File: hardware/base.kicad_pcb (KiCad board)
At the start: 4 copper layers, 100 x 85 mm, 316 parts, among them J101 USB-A, J102 TNG-Data-TOP, J103 TNG-Power-TOP, J301 MICROSDCARD, J302 Raspberry-Pi-Compute-Socket, J303 MICRO_HDMI, J304 USB Micro, J401 RJSLG-001TA1, P101 Debug, P102 Boot, P103 PE, P104 TST_GND, P105 TST_3V3P, P201 DI IN, P202 PWR IN, P203 TST_5V, P204 TST_GND, P301 TST_XMC_10, P302 TST_SCL, P303 TST_SDA, P304 TST_WP, P305 TST_3V3, P306 TST_1V8, P307 TST_XMC_11, P401 TST_1V2, Q301 2N7002P, Q302 2N7002P, Q303 2N7002P, Q304 2N7002P, Q305 2N7002P, T201 744272251, U101 USB2517, U102 MIC2026-1YM, U103 82400152, U104 XMC1XXX24, U105 TPD4S010DQA, U106 TPD4S010DQA, U107 TPD4S010DQA, U108 AP7333-33SAG-7, U109 TPS22975, U110 TPS22975, U111 PCT2075DP, U112 VN7140AS, U201 ISO1211, U202 FPF2700MX, U203 BD90640HFP, U204 PAC1933, U301 PAM2306AYPAA, U302 PCF8523T, U303 FSUSB42MUX, U304 TPD4S010DQA, U305 TPD4S010DQA, U306 TPD4S010DQA, U307 82400152, U308 M24256-DFMN6TP, U309 AP2331, U310 SLB9670, U401 LAN7500, U402 93AA66, U403 TPD4S010DQA, U404 TPD4S010DQA, U405 PAM2306AYPAA, X101 24MHz, X301 32.768kHz, X401 25MHz_18pF

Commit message: fix text
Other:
- board text added: "BASE RPI CMX REV 1.2"
- board text removed: "Base RPI CMX REV 1.2"

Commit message: specify capacitor voltages
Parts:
- C201, C202: value 10uF -> 10uF/35V
- C205: value 100nF -> 100nF/35V

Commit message: fix capacitor footprints
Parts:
- C135, C136: footprint C1206 -> kicad-libraries:C0805E
- C203: value 10uF -> 10uF/35V
- C219: value >100µF -> 100µF
- moved C135 0.40 mm to (153.7, 78.4)
- moved C136 0.40 mm to (153.7, 80.6)

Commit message: fix capacitor values
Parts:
- C108, C109, C117: value >100uF -> 100uF
- C216, C220: value >100µF -> 100µF

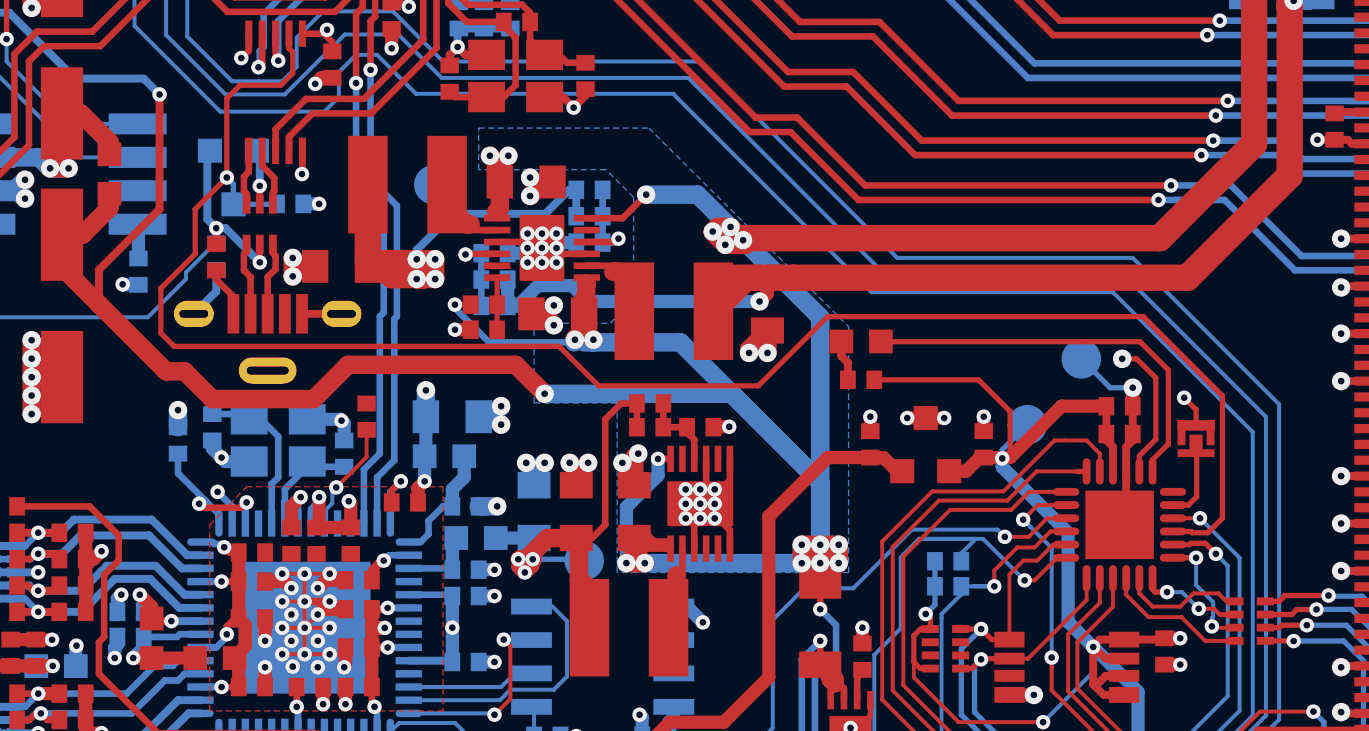
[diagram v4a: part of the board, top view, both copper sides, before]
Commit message: fix footprints
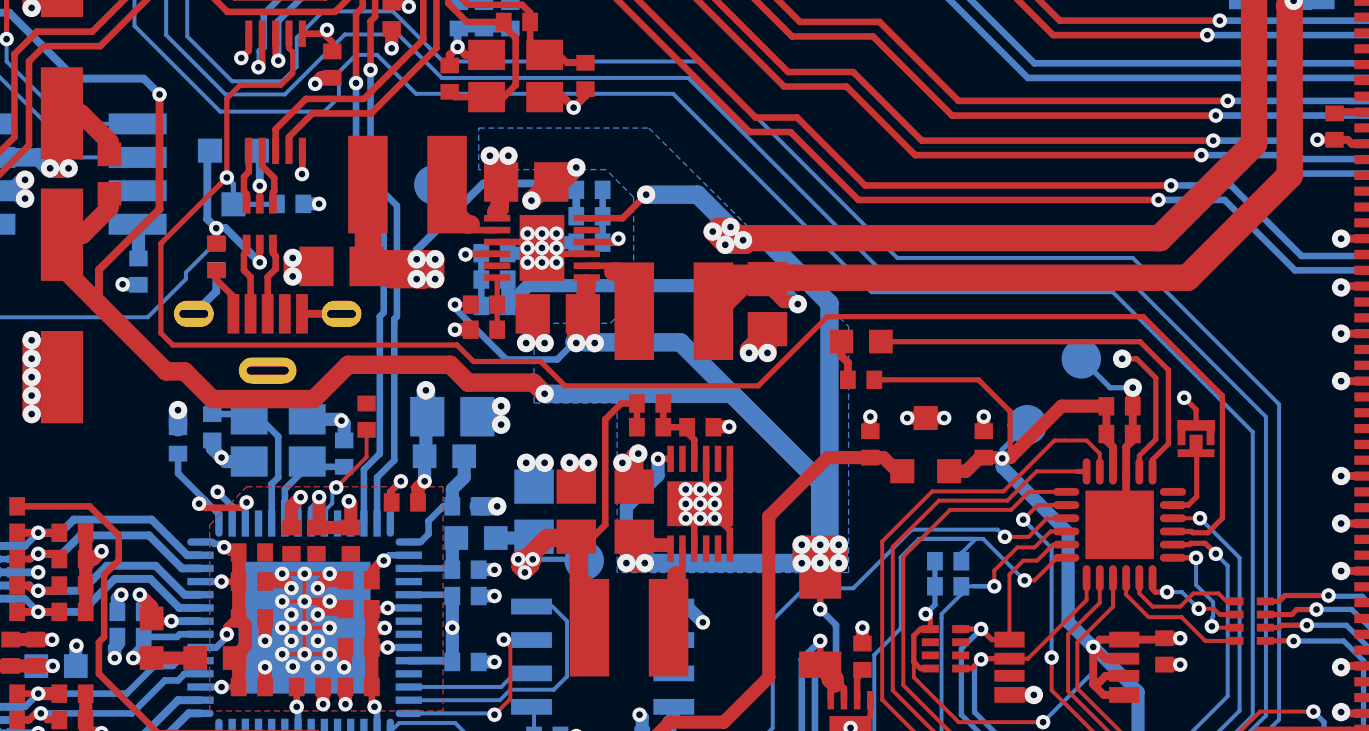
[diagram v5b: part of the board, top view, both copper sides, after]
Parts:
- C301, C303, C309, C311, C401, C410, C435, C437: footprint C0805 -> kicad-libraries:C0805E
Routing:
- net +1.8V: track 124.2 -> 126.4 mm
- net 5VSW: track 251.9 -> 253.4 mm
- net AGND: track 1114.5 -> 1115.5 mm

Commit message: fix footprint
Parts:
- R118: footprint kicad-libraries:1206 -> kicad-libraries:R1206

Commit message: fix values
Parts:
- C127, C128, C307, C308, C310, C320: value 1µF -> 1uF
- C216, C219, C220: value 100µF -> 100uF
- C301, C303, C309, C311, C435, C437: value 10µF -> 10uF
- C304, C312, C313, C314: value 47µF -> 47uF
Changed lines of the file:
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@@
       (effects (font (size 0.3 0.3) (thickness 0.075)) (justify mirror))
     )
-    (fp_text value 47µF (at 0 0.65 180) (layer B.Fab)
+    (fp_text value 47uF (at 0 0.65 180) (layer B.Fab)
       (effects (font (size 0.3 0.3) (thickness 0.075)) (justify mirror))
     )
@@
       (effects (font (size 0.3 0.3) (thickness 0.075)) (justify mirror))
     )
-    (fp_text value 47µF (at 0 0.65 180) (layer B.Fab)
+    (fp_text value 47uF (at 0 0.65 180) (layer B.Fab)
       (effects (font (size 0.3 0.3) (thickness 0.075)) (justify mirror))
     )
@@
       (effects (font (size 0.3 0.3) (thickness 0.075)) (justify mirror))
     )
-    (fp_text value 47µF (at 0 0.65 180) (layer B.Fab)
+    (fp_text value 47uF (at 0 0.65 180) (layer B.Fab)
       (effects (font (size 0.3 0.3) (thickness 0.075)) (justify mirror))
     )
@@
       (effects (font (size 0.2 0.2) (thickness 0.05)))
     )
-    (fp_text value 1µF (at 0 -0.15 270) (layer F.Fab)
+    (fp_text value 1uF (at 0 -0.15 270) (layer F.Fab)
       (effects (font (size 0.2 0.2) (thickness 0.05)))
     )
@@
       (effects (font (size 0.2 0.2) (thickness 0.05)))
     )
-    (fp_text value 1µF (at 0 -0.15) (layer F.Fab)
+    (fp_text value 1uF (at 0 -0.15) (layer F.Fab)
       (effects (font (size 0.2 0.2) (thickness 0.05)))
     )
@@
       (effects (font (size 0.59944 0.59944) (thickness 0.12446)))
     )
-    (fp_text value 100µF (at 0.95 -0.375 90) (layer F.Fab)
+    (fp_text value 100uF (at 0.95 -0.375 90) (layer F.Fab)
       (effects (font (size 0.59944 0.59944) (thickness 0.12446)))
     )
@@
       (effects (font (size 0.59944 0.59944) (thickness 0.12446)))
     )
-    (fp_text value 100µF (at 0.95 -0.375 90) (layer F.Fab)
+    (fp_text value 100uF (at 0.95 -0.375 90) (layer F.Fab)
       (effects (font (size 0.59944 0.59944) (thickness 0.12446)))
     )
@@
       (effects (font (size 0.59944 0.59944) (thickness 0.12446)))
     )
-    (fp_text value 100µF (at 0.95 -0.375 90) (layer F.Fab)
+    (fp_text value 100uF (at 0.95 -0.375 90) (layer F.Fab)
       (effects (font (size 0.59944 0.59944) (thickness 0.12446)))
     )
@@
       (effects (font (size 0.2 0.2) (thickness 0.05)))
     )
-    (fp_text value 1µF (at 0.05 -0.375 90) (layer F.Fab)
+    (fp_text value 1uF (at 0.05 -0.375 90) (layer F.Fab)
       (effects (font (size 0.2 0.2) (thickness 0.05)))
     )
@@
       (effects (font (size 0.2 0.2) (thickness 0.05)))
     )
-    (fp_text value 1µF (at 0 -0.15 90) (layer F.Fab)
+    (fp_text value 1uF (at 0 -0.15 90) (layer F.Fab)
       (effects (font (size 0.2 0.2) (thickness 0.05)))
     )
@@
       (effects (font (size 0.2 0.2) (thickness 0.05)))
     )
-    (fp_text value 1µF (at 0 -0.15 90) (layer F.Fab)
+    (fp_text value 1uF (at 0 -0.15 90) (layer F.Fab)
       (effects (font (size 0.2 0.2) (thickness 0.05)))
     )
@@
       (effects (font (size 0.2 0.2) (thickness 0.05)))
     )
-    (fp_text value 1µF (at 0 -0.15 90) (layer F.Fab)
+    (fp_text value 1uF (at 0 -0.15 90) (layer F.Fab)
       (effects (font (size 0.2 0.2) (thickness 0.05)))
     )
@@
       (effects (font (size 0.2 0.2) (thickness 0.05)))
     )
-    (fp_text value 47µF (at 0 -0.4 90) (layer F.Fab)
+    (fp_text value 47uF (at 0 -0.4 90) (layer F.Fab)
       (effects (font (size 0.2 0.2) (thickness 0.05)))
     )
@@
       (effects (font (size 0.2 0.2) (thickness 0.05)))
     )
-    (fp_text value 10µF (at 0 -0.4) (layer F.Fab)
+    (fp_text value 10uF (at 0 -0.4) (layer F.Fab)
       (effects (font (size 0.2 0.2) (thickness 0.05)))
     )
@@
       (effects (font (size 0.2 0.2) (thickness 0.05)))
     )
-    (fp_text value 10µF (at 0 -0.4 90) (layer F.Fab)
+    (fp_text value 10uF (at 0 -0.4 90) (layer F.Fab)
       (effects (font (size 0.2 0.2) (thickness 0.05)))
     )
@@
       (effects (font (size 0.2 0.2) (thickness 0.05)))
     )
-    (fp_text value 10µF (at 0 -0.4 90) (layer F.Fab)
+    (fp_text value 10uF (at 0 -0.4 90) (layer F.Fab)
       (effects (font (size 0.2 0.2) (thickness 0.05)))
     )
@@
       (effects (font (size 0.2 0.2) (thickness 0.05)))
     )
-    (fp_text value 10µF (at 0 -0.4) (layer F.Fab)
+    (fp_text value 10uF (at 0 -0.4) (layer F.Fab)
       (effects (font (size 0.2 0.2) (thickness 0.05)))
     )
@@
       (effects (font (size 0.2 0.2) (thickness 0.05)))
     )
-    (fp_text value 10µF (at 0 -0.4) (layer F.Fab)
+    (fp_text value 10uF (at 0 -0.4) (layer F.Fab)
       (effects (font (size 0.2 0.2) (thickness 0.05)))
     )
@@
       (effects (font (size 0.2 0.2) (thickness 0.05)))
     )
-    (fp_text value 10µF (at 0 -0.4 90) (layer F.Fab)
+    (fp_text value 10uF (at 0 -0.4 90) (layer F.Fab)
       (effects (font (size 0.2 0.2) (thickness 0.05)))
     )

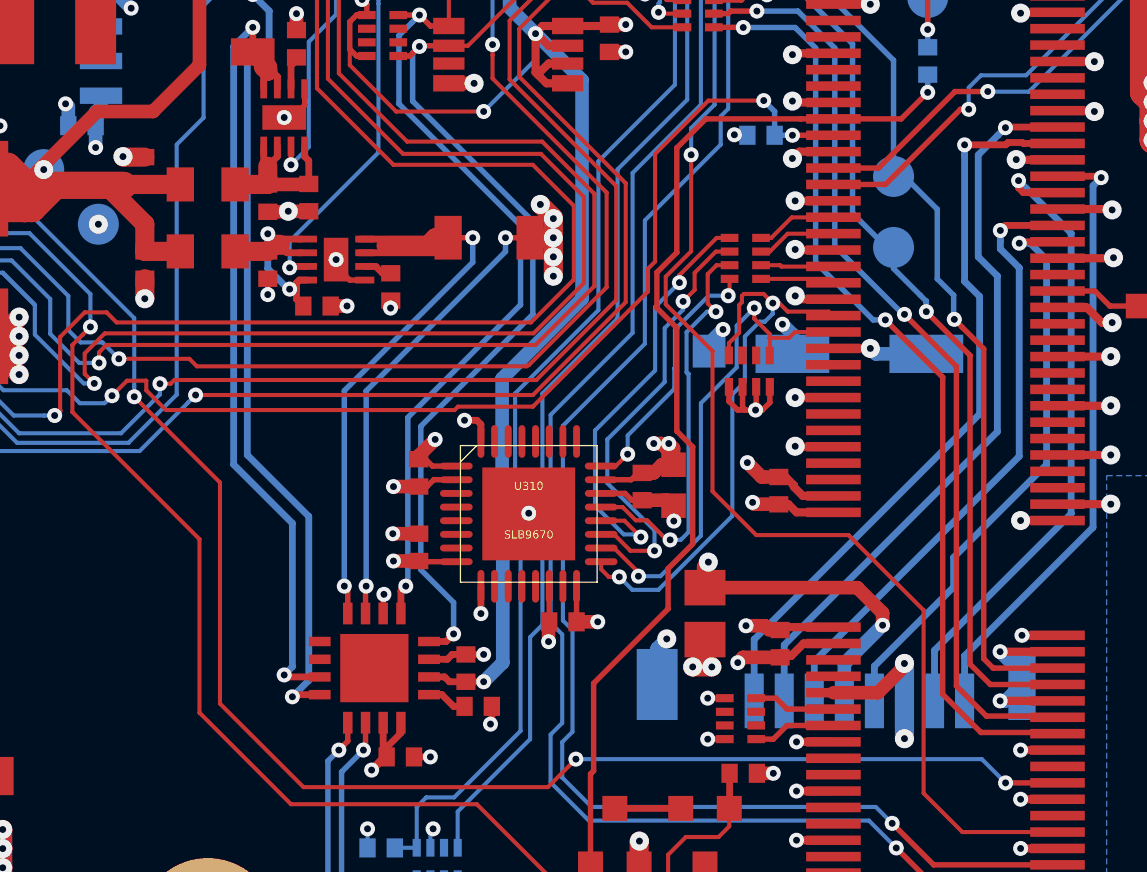
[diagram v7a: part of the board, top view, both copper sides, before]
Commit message: fix footprints
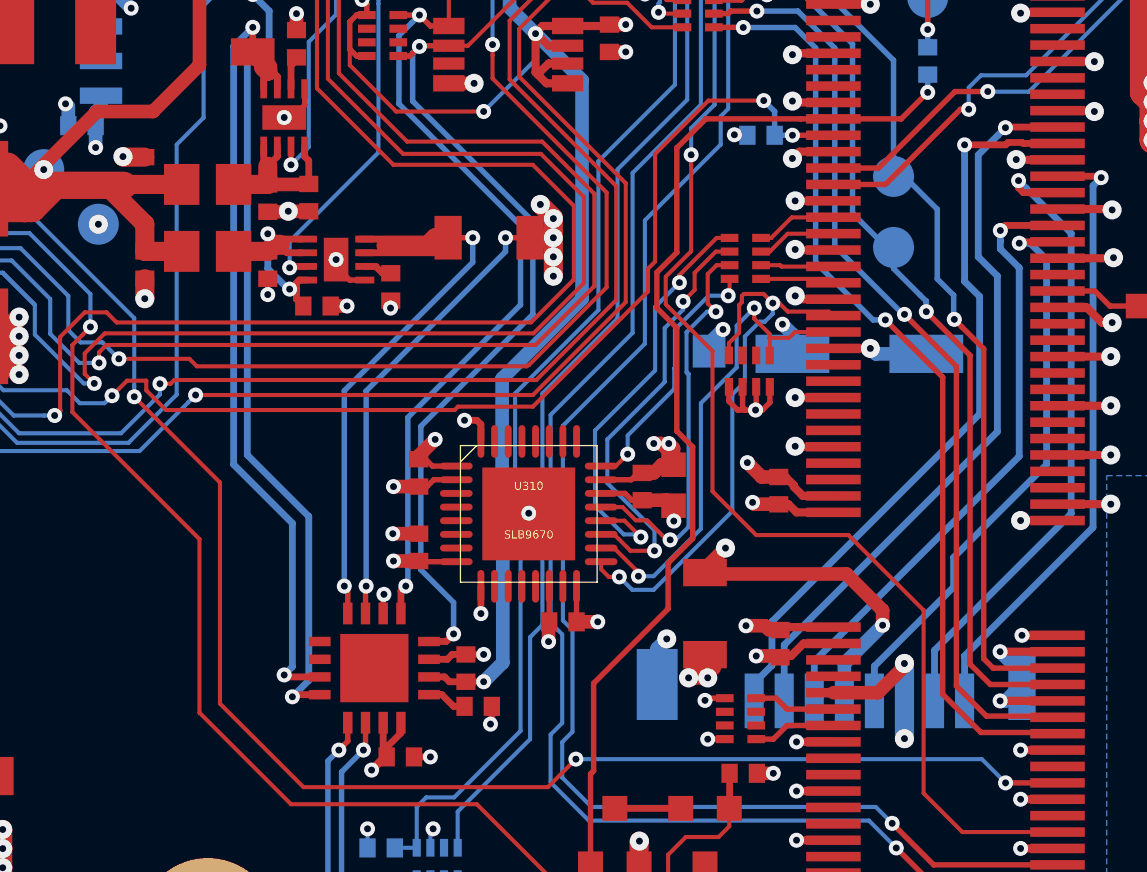
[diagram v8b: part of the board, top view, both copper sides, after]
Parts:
- C304: footprint kicad-libraries:C0805E -> kicad-libraries:C1206
- L108, L109: footprint kicad-libraries:R0805 -> kicad-libraries:R0805E
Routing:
- net AGND: track 1115.5 -> 1114.9 mm
